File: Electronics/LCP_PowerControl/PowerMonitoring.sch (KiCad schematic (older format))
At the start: 18 parts, among them Q1 2N7002, Q2 2N7002, U1 MAX17205

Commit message: Adding libraries and recent changes
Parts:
- added J?: Conn_02x04_Odd_Even, Connector_PinSocket_2.54mm:PinSocket_2x04_P2.54mm_Vertical, symbol Connector_Generic:Conn_02x04_Odd_Even
- added TP? (x2): TestPoint, TestPoint:TestPoint_Keystone_5000-5004_Miniature, symbol Connector:TestPoint
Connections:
- wire segments 64 -> 82
- no-connect marks 0 -> 1
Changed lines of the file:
@@
 $Descr A4 11693 8268
 encoding utf-8
-Sheet 3 8
+Sheet 3 11
 Title ""
 Date ""
@@
 Connection ~ 5450 5300
 Wire Wire Line
-	1650 5300 5450 5300
+	1650 5300 3450 5300
 Text HLabel 1600 2300 0    50   Input ~ 0
 BATT_V+
@@
 BM_SDA
 Wire Wire Line
-	10350 3250 8900 3250
+	10350 3250 9600 3250
 Text HLabel 10350 3500 2    50   Input ~ 0
 BM_SCL
@@
 BM_IRQ
 Wire Wire Line
-	10350 3500 8900 3500
-Wire Wire Line
-	8900 3750 10350 3750
+	10350 3500 9500 3500
 Wire Wire Line
 	4000 3600 5400 3600
@@
 	8150 2300 8150 2050
 Wire Wire Line
-	4900 2300 8150 2300
+	4900 2300 6600 2300
+$Comp
+L power:GND #PWR?
+U 1 1 5EEDB371
+P 9400 5100
+AR Path="/5EE2AA1B/5EEDB371" Ref="#PWR?"  Part="1"
+AR Path="/5EE2A7AF/5EEDB371" Ref="#PWR?"  Part="1"
+F 0 "#PWR?" H 9400 4850 50  0001 C CNN
+F 1 "GND" H 9405 4927 50  0000 C CNN
+F 2 "" H 9400 5100 50  0001 C CNN
+F 3 "" H 9400 5100 50  0001 C CNN
+	1    9400 5100
+	1    0    0    -1
+$EndComp
+Wire Wire Line
+	9400 5100 9400 4950
+Wire Wire Line
+	9500 4900 9500 4950
+Wire Wire Line
+	9500 4950 9400 4950
+Connection ~ 9400 4950
+Wire Wire Line
+	9400 4950 9400 4900
+Wire Wire Line
+	9600 4900 9600 4950
+Connection ~ 9500 4950
+$Comp
+L Connector_Generic:Conn_02x04_Odd_Even J?
+U 1 1 5EEDB37F
+P 9500 4600
+AR Path="/5EE2AA1B/5EEDB37F" Ref="J?"  Part="1"
+AR Path="/5EE2A7AF/5EEDB37F" Ref="J?"  Part="1"
+F 0 "J?" V 9459 4312 50  0000 R CNN
+F 1 "Conn_02x04_Odd_Even" V 9550 4312 50  0000 R CNN
+F 2 "Connector_PinSocket_2.54mm:PinSocket_2x04_P2.54mm_Vertical" H 9500 4600 50  0001 C CNN
+F 3 "~" H 9500 4600 50  0001 C CNN
+F 4 "SALEAE_TEST" V 9641 4312 50  0000 R CNN "Field4"
+	1    9500 4600
+	0    -1   1    0
+$EndComp
+Wire Wire Line
+	9700 4900 9700 4950
+Wire Wire Line
+	9500 4950 9600 4950
+Wire Wire Line
+	9600 4950 9700 4950
+Connection ~ 9600 4950
+Wire Wire Line
+	9400 4400 9400 3750
+Wire Wire Line
+	8900 3750 9400 3750
+Connection ~ 9400 3750
+Wire Wire Line
+	9400 3750 10350 3750
+Wire Wire Line
+	9500 4400 9500 3500
+Connection ~ 9500 3500
+Wire Wire Line
+	9500 3500 8900 3500
+Wire Wire Line
+	9600 4400 9600 3250
+Connection ~ 9600 3250
+Wire Wire Line
+	9600 3250 8900 3250
+NoConn ~ 9700 4400
+$Comp
+L Connector:TestPoint TP?
+U 1 1 5EE905FF
+P 6600 2200
+F 0 "TP?" H 6658 2318 50  0000 L CNN
+F 1 "TestPoint" H 6658 2227 50  0000 L CNN
+F 2 "TestPoint:TestPoint_Keystone_5000-5004_Miniature" H 6800 2200 50  0001 C CNN
+F 3 "~" H 6800 2200 50  0001 C CNN
+F 4 "5000" H 6600 2200 50  0001 C CNN "MPN"
+	1    6600 2200
+	1    0    0    -1
+$EndComp
+Wire Wire Line
+	6600 2200 6600 2300
+Connection ~ 6600 2300
+Wire Wire Line
+	6600 2300 8150 2300
+$Comp
+L Connector:TestPoint TP?
+U 1 1 5EE92BE6
+P 3450 5250
+F 0 "TP?" H 3508 5368 50  0000 L CNN
+F 1 "TestPoint" H 3508 5277 50  0000 L CNN
+F 2 "TestPoint:TestPoint_Keystone_5000-5004_Miniature" H 3650 5250 50  0001 C CNN
+F 3 "~" H 3650 5250 50  0001 C CNN
+F 4 "5001" H 3450 5250 50  0001 C CNN "MPN"
+	1    3450 5250
+	1    0    0    -1
+$EndComp
+Wire Wire Line
+	3450 5250 3450 5300
+Connection ~ 3450 5300
+Wire Wire Line
+	3450 5300 5450 5300
 $EndSCHEMATC

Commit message: Aiming for rev 0.1 complete
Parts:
- R6, R7, R8: footprint (none) -> Resistor_SMD:R_0805_2012Metric
- gave numbers to parts that had none: 3
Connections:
- wire segments 82 -> 87
- no-connect marks 1 -> 4
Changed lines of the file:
@@
 Sheet 3 11
 Title ""
-Date ""
-Rev ""
+Date "2020-06-17"
+Rev "R0.1"
 Comp ""
-Comment1 ""
+Comment1 "Design by: Matt Casari"
 Comment2 ""
 Comment3 ""
@@
 F 0 "R6" V 8650 3250 50  0000 C CNN
 F 1 "1k" V 8750 3250 50  0000 C CNN
-F 2 "" V 8680 3250 50  0001 C CNN
+F 2 "Resistor_SMD:R_0805_2012Metric" V 8680 3250 50  0001 C CNN
 F 3 "~" H 8750 3250 50  0001 C CNN
 	1    8750 3250
@@
 F 0 "R7" V 8650 3500 50  0000 C CNN
 F 1 "150" V 8750 3500 50  0000 C CNN
-F 2 "" V 8680 3500 50  0001 C CNN
+F 2 "Resistor_SMD:R_0805_2012Metric" V 8680 3500 50  0001 C CNN
 F 3 "~" H 8750 3500 50  0001 C CNN
 	1    8750 3500
@@
 F 0 "R8" V 8650 3750 50  0000 C CNN
 F 1 "150" V 8750 3750 50  0000 C CNN
-F 2 "" V 8680 3750 50  0001 C CNN
+F 2 "Resistor_SMD:R_0805_2012Metric" V 8680 3750 50  0001 C CNN
 F 3 "~" H 8750 3750 50  0001 C CNN
 	1    8750 3750
@@
 	5050 3350 4900 3350
 Wire Wire Line
-	5400 3200 5200 3200
-Wire Wire Line
 	5200 3200 5200 3000
 Wire Wire Line
@@
 L power:+BATT #PWR07
 U 1 1 5EE801D6
-P 8150 2050
-F 0 "#PWR07" H 8150 1900 50  0001 C CNN
-F 1 "+BATT" H 8165 2223 50  0000 C CNN
-F 2 "" H 8150 2050 50  0001 C CNN
-F 3 "" H 8150 2050 50  0001 C CNN
-	1    8150 2050
-	1    0    0    -1
-$EndComp
-Wire Wire Line
-	8150 2300 8150 2050
+P 8150 2150
+F 0 "#PWR07" H 8150 2000 50  0001 C CNN
+F 1 "+BATT" H 8165 2323 50  0000 C CNN
+F 2 "" H 8150 2150 50  0001 C CNN
+F 3 "" H 8150 2150 50  0001 C CNN
+	1    8150 2150
+	1    0    0    -1
+$EndComp
+Wire Wire Line
+	8150 2300 8150 2150
 Wire Wire Line
 	4900 2300 6600 2300
@@
 P 9400 5100
 AR Path="/5EE2AA1B/5EEDB371" Ref="#PWR?"  Part="1"
-AR Path="/5EE2A7AF/5EEDB371" Ref="#PWR?"  Part="1"
-F 0 "#PWR?" H 9400 4850 50  0001 C CNN
+AR Path="/5EE2A7AF/5EEDB371" Ref="#PWR032"  Part="1"
+F 0 "#PWR032" H 9400 4850 50  0001 C CNN
 F 1 "GND" H 9405 4927 50  0000 C CNN
 F 2 "" H 9400 5100 50  0001 C CNN
@@
 P 9500 4600
 AR Path="/5EE2AA1B/5EEDB37F" Ref="J?"  Part="1"
-AR Path="/5EE2A7AF/5EEDB37F" Ref="J?"  Part="1"
-F 0 "J?" V 9459 4312 50  0000 R CNN
+AR Path="/5EE2A7AF/5EEDB37F" Ref="J13"  Part="1"
+F 0 "J13" V 9459 4312 50  0000 R CNN
 F 1 "Conn_02x04_Odd_Even" V 9550 4312 50  0000 R CNN
 F 2 "Connector_PinSocket_2.54mm:PinSocket_2x04_P2.54mm_Vertical" H 9500 4600 50  0001 C CNN
@@
 NoConn ~ 9700 4400
 $Comp
-L Connector:TestPoint TP?
+L Connector:TestPoint TP2
 U 1 1 5EE905FF
 P 6600 2200
-F 0 "TP?" H 6658 2318 50  0000 L CNN
+F 0 "TP2" H 6658 2318 50  0000 L CNN
 F 1 "TestPoint" H 6658 2227 50  0000 L CNN
 F 2 "TestPoint:TestPoint_Keystone_5000-5004_Miniature" H 6800 2200 50  0001 C CNN
@@
 Connection ~ 6600 2300
 Wire Wire Line
-	6600 2300 8150 2300
-$Comp
-L Connector:TestPoint TP?
+	6600 2300 7450 2300
+$Comp
+L Connector:TestPoint TP1
 U 1 1 5EE92BE6
 P 3450 5250
-F 0 "TP?" H 3508 5368 50  0000 L CNN
+F 0 "TP1" H 3508 5368 50  0000 L CNN
 F 1 "TestPoint" H 3508 5277 50  0000 L CNN
 F 2 "TestPoint:TestPoint_Keystone_5000-5004_Miniature" H 3650 5250 50  0001 C CNN
@@
 Wire Wire Line
 	3450 5300 5450 5300
+$Comp
+L power:PWR_FLAG #FLG0101
+U 1 1 5EEBFECA
+P 7450 2200
+F 0 "#FLG0101" H 7450 2275 50  0001 C CNN
+F 1 "PWR_FLAG" H 7450 2373 50  0000 C CNN
+F 2 "" H 7450 2200 50  0001 C CNN
+F 3 "~" H 7450 2200 50  0001 C CNN
+	1    7450 2200
+	1    0    0    -1
+$EndComp
+Wire Wire Line
+	7450 2200 7450 2300
+Connection ~ 7450 2300
+Wire Wire Line
+	7450 2300 8150 2300
+$Comp
+L power:PWR_FLAG #FLG0102
+U 1 1 5EEC41BF
+P 5550 2800
+F 0 "#FLG0102" H 5550 2875 50  0001 C CNN
+F 1 "PWR_FLAG" H 5550 2973 50  0000 C CNN
+F 2 "" H 5550 2800 50  0001 C CNN
+F 3 "~" H 5550 2800 50  0001 C CNN
+	1    5550 2800
+	1    0    0    -1
+$EndComp
+Wire Wire Line
+	5550 2800 5550 2900
+Wire Wire Line
+	5200 3200 5400 3200
+Wire Wire Line
+	5200 3000 5200 2900
+Wire Wire Line
+	5200 2900 5550 2900
+Connection ~ 5200 3000
+NoConn ~ 5400 4050
+NoConn ~ 5400 4200
+NoConn ~ 5400 4400
 $EndSCHEMATC

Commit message: KiCad Layout
Component and Traces finished. Need a look over. Will work on Silkscreen
after.

JTAG Connector. Should pin 1 be pulled up w/ 470Ohm resistor similar to
other designs? Also TDI and TMI signals are connected, is this correct?
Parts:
- U1: symbol PMEL_BatteryManagement:MAX17205 -> LCP_PowerControl-rescue:MAX17205-PMEL_BatteryManagement
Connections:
- wire segments 87 -> 86
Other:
- moved on the sheet: R5
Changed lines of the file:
@@
 $EndDescr
 $Comp
-L PMEL_BatteryManagement:MAX17205 U1
+L LCP_PowerControl-rescue:MAX17205-PMEL_BatteryManagement U1
 U 1 1 5EE2E9B5
 P 5950 3700
+AR Path="/5EE2E9B5" Ref="U1"  Part="1"
+AR Path="/5EE2A7AF/5EE2E9B5" Ref="U1"  Part="1"
 F 0 "U1" H 5925 4515 50  0000 C CNN
 F 1 "MAX17205" H 5925 4424 50  0000 C CNN
@@
 L Device:R R5
 U 1 1 5EE309A9
-P 5700 5300
-F 0 "R5" V 5600 5300 50  0000 C CNN
-F 1 "0.25" V 5800 5300 50  0000 C CNN
-F 2 "Resistor_THT:R_Axial_Power_L48.0mm_W12.5mm_P55.88mm" V 5630 5300 50  0001 C CNN
-F 3 "~" H 5700 5300 50  0001 C CNN
-F 4 "RS010R2500FE73" V 5700 5300 50  0001 C CNN "MPN"
-F 5 "10W" V 5700 5300 50  0000 C CNN "Power"
-	1    5700 5300
-	0    1    1    0
-$EndComp
-Wire Wire Line
-	5850 5300 6200 5300
+P 5950 5300
+F 0 "R5" V 5850 5300 50  0000 C CNN
+F 1 "0.25" V 6050 5300 50  0000 C CNN
+F 2 "Resistor_THT:R_Axial_Power_L48.0mm_W12.5mm_P55.88mm" V 5880 5300 50  0001 C CNN
+F 3 "~" H 5950 5300 50  0001 C CNN
+F 4 "RS010R2500FE73" V 5950 5300 50  0001 C CNN "MPN"
+F 5 "10W" V 5950 5300 50  0000 C CNN "Power"
+	1    5950 5300
+	0    1    1    0
+$EndComp
+Wire Wire Line
+	6100 5300 6200 5300
 Connection ~ 6200 5300
 Wire Wire Line
-	5700 5000 5450 5000
-Wire Wire Line
-	5450 5000 5450 5300
-Wire Wire Line
-	5450 5300 5550 5300
-Wire Wire Line
-	5950 5000 5700 5000
-Connection ~ 5700 5000
+	5700 5300 5800 5300
 $Comp
 L Transistor_FET:2N7002 Q1
@@
 Text HLabel 1650 5300 0    50   Output ~ 0
 BATT_V-
-Connection ~ 5450 5300
+Connection ~ 5700 5300
 Wire Wire Line
 	1650 5300 3450 5300
@@
 Connection ~ 3700 3800
 Wire Wire Line
-	6200 4850 6200 5300
-Wire Wire Line
-	5950 4850 5950 5000
-Wire Wire Line
-	5700 4850 5700 5000
+	6200 4850 6200 5000
 $Comp
 L power:GND #PWR01
@@
 Connection ~ 3450 5300
 Wire Wire Line
-	3450 5300 5450 5300
+	3450 5300 5700 5300
 $Comp
 L power:PWR_FLAG #FLG0101
@@
 NoConn ~ 5400 4200
 NoConn ~ 5400 4400
+Wire Wire Line
+	5950 4850 5950 5000
+Wire Wire Line
+	5950 5000 6200 5000
+Connection ~ 6200 5000
+Wire Wire Line
+	6200 5000 6200 5300
+Wire Wire Line
+	5700 4850 5700 5300
 $EndSCHEMATC

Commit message: Position request within 0.005 inches working
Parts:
- U1: symbol LCP_PowerControl-rescue:MAX17205-PMEL_BatteryManagement -> LCP_PowerControl-rescue:MAX17205-PMEL_BatteryManagement-LCP_PowerControl-rescue
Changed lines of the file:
@@
 $EndDescr
 $Comp
-L LCP_PowerControl-rescue:MAX17205-PMEL_BatteryManagement U1
+L LCP_PowerControl-rescue:MAX17205-PMEL_BatteryManagement-LCP_PowerControl-rescue U1
 U 1 1 5EE2E9B5
 P 5950 3700

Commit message: LCP_PowerControl Rev1
Board layout in Kicad.
Gerbers.
BOM
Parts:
- C1: MPN (none) -> C1206X7R101-105KNE
- C2, C3: MPN (none) -> 885012207102
- R3: MPN (none) -> CRCW0805200KJNEA
- R6: MPN (none) -> RNCP0805FTD1K00
- R7, R8: MPN (none) -> RNCP0805FTD150R
- renumbered Q1 to e
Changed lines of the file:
@@
 	5700 5300 5800 5300
 $Comp
-L Transistor_FET:2N7002 Q1
+L Transistor_FET:2N7002 e
 U 1 1 5EE31D3D
 P 3800 3600
-F 0 "Q1" H 4005 3646 50  0000 L CNN
+F 0 "e" H 4005 3646 50  0000 L CNN
 F 1 "2N7002" H 4005 3555 50  0000 L CNN
 F 2 "Package_TO_SOT_SMD:SOT-23" H 4000 3525 50  0001 L CIN
@@
 F 2 "Resistor_SMD:R_0805_2012Metric" V 8680 3250 50  0001 C CNN
 F 3 "~" H 8750 3250 50  0001 C CNN
+F 4 "RNCP0805FTD1K00" V 8750 3250 50  0001 C CNN "MPN"
 	1    8750 3250
 	0    1    1    0
@@
 F 2 "Resistor_SMD:R_0805_2012Metric" V 8680 3500 50  0001 C CNN
 F 3 "~" H 8750 3500 50  0001 C CNN
+F 4 "RNCP0805FTD150R" V 8750 3500 50  0001 C CNN "MPN"
 	1    8750 3500
 	0    1    1    0
@@
 F 2 "Resistor_SMD:R_0805_2012Metric" V 8680 3750 50  0001 C CNN
 F 3 "~" H 8750 3750 50  0001 C CNN
+F 4 "RNCP0805FTD150R" V 8750 3750 50  0001 C CNN "MPN"
 	1    8750 3750
 	0    1    1    0
@@
 F 2 "Resistor_SMD:R_0805_2012Metric" V 3630 4050 50  0001 C CNN
 F 3 "~" H 3700 4050 50  0001 C CNN
+F 4 "CRCW0805200KJNEA" H 3700 4050 50  0001 C CNN "MPN"
 	1    3700 4050
 	1    0    0    -1
@@
 	1    0    0    -1
 $EndComp
-$Comp
-L Device:R R4
-U 1 1 5EE5DDEB
-P 4350 2550
-F 0 "R4" H 4420 2596 50  0000 L CNN
-F 1 "500k" H 4420 2505 50  0000 L CNN
-F 2 "Resistor_SMD:R_0805_2012Metric" V 4280 2550 50  0001 C CNN
-F 3 "~" H 4350 2550 50  0001 C CNN
-F 4 "CRCW08058M87FKEA" H 4350 2550 50  0001 C CNN "MPN"
-	1    4350 2550
-	1    0    0    -1
-$EndComp
 Wire Wire Line
 	4600 2750 4350 2750
@@
 F 2 "Capacitor_SMD:C_0805_2012Metric" H 6738 4450 50  0001 C CNN
 F 3 "~" H 6700 4600 50  0001 C CNN
+F 4 "885012207102" H 6700 4600 50  0001 C CNN "MPN"
 	1    6700 4600
 	1    0    0    -1
@@
 F 2 "Capacitor_SMD:C_0805_2012Metric" H 7188 4450 50  0001 C CNN
 F 3 "~" H 7150 4600 50  0001 C CNN
+F 4 "885012207102" H 7150 4600 50  0001 C CNN "MPN"
 	1    7150 4600
 	1    0    0    -1
@@
 F 2 "Capacitor_SMD:C_0805_2012Metric" H 4938 3000 50  0001 C CNN
 F 3 "~" H 4900 3150 50  0001 C CNN
+F 4 "C1206X7R101-105KNE" H 4900 3150 50  0001 C CNN "MPN"
 	1    4900 3150
 	1    0    0    -1
@@
 Wire Wire Line
 	5700 4850 5700 5300
+$Comp
+L Device:R R4
+U 1 1 5EE5DDEB
+P 4350 2550
+F 0 "R4" H 4420 2596 50  0000 L CNN
+F 1 "500k" H 4420 2505 50  0000 L CNN
+F 2 "Resistor_SMD:R_0805_2012Metric" V 4280 2550 50  0001 C CNN
+F 3 "~" H 4350 2550 50  0001 C CNN
+F 4 "CRCW08058M87FKEA" H 4350 2550 50  0001 C CNN "MPN"
+	1    4350 2550
+	1    0    0    -1
+$EndComp
 $EndSCHEMATC

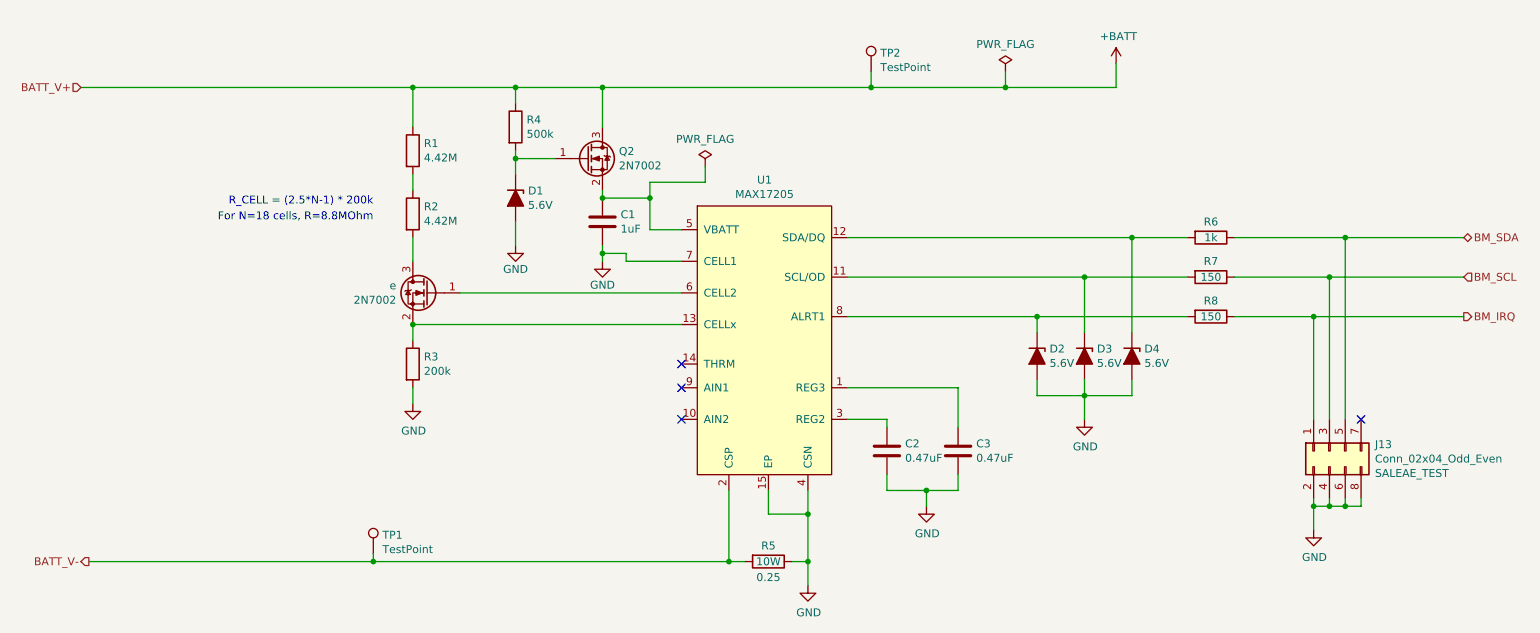
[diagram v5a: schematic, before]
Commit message: Rev1
Removed test points. Cleaned up unnecessary traces. Fixed electrical issues #1-#7
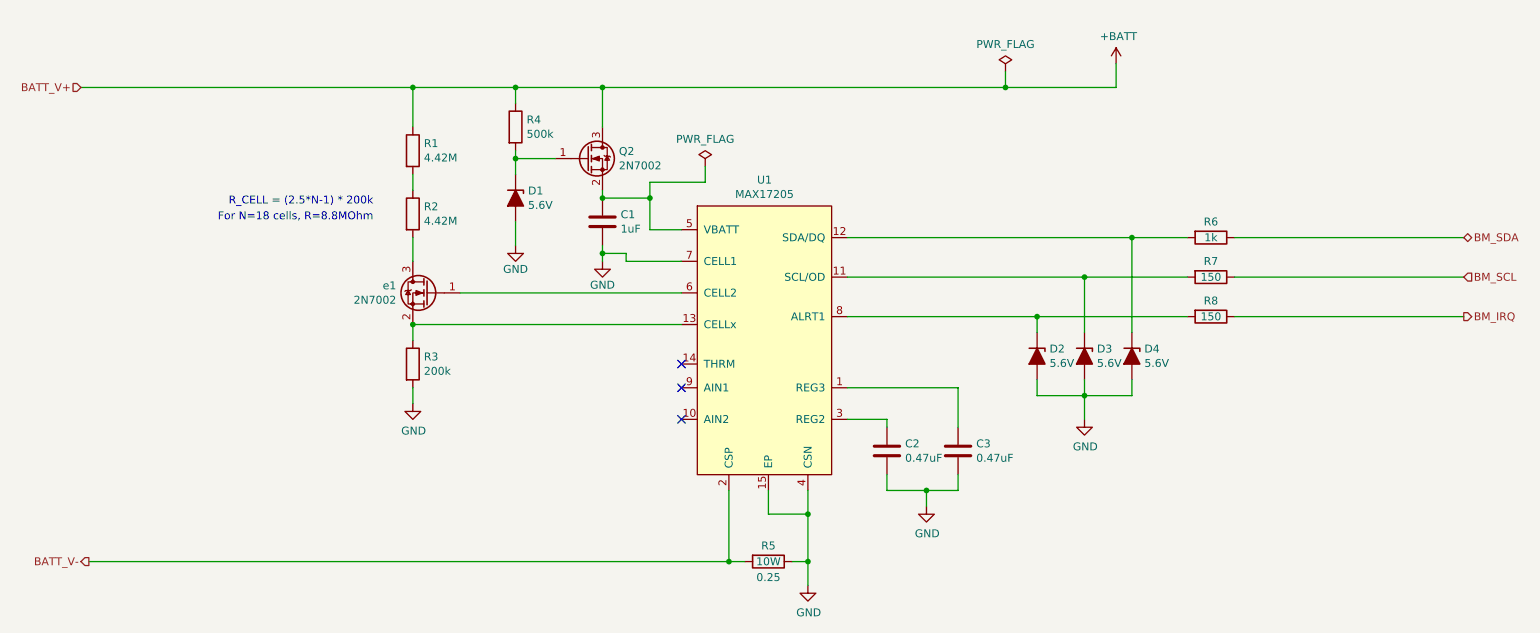
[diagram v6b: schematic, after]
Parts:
- removed J13: Conn_02x04_Odd_Even, Connector_PinSocket_2.54mm:PinSocket_2x04_P2.54mm_Vertical, symbol Connector_Generic:Conn_02x04_Odd_Even
- removed TP1, TP2: TestPoint, TestPoint:TestPoint_Keystone_5000-5004_Miniature, symbol Connector:TestPoint
- renumbered e to e1
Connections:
- no-connect marks 4 -> 3
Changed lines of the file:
@@
 	5700 5300 5800 5300
 $Comp
-L Transistor_FET:2N7002 e
+L Transistor_FET:2N7002 e1
 U 1 1 5EE31D3D
 P 3800 3600
-F 0 "e" H 4005 3646 50  0000 L CNN
+F 0 "e1" H 4005 3646 50  0000 L CNN
 F 1 "2N7002" H 4005 3555 50  0000 L CNN
 F 2 "Package_TO_SOT_SMD:SOT-23" H 4000 3525 50  0001 L CIN
@@
 BATT_V-
 Connection ~ 5700 5300
-Wire Wire Line
-	1650 5300 3450 5300
 Text HLabel 1600 2300 0    50   Input ~ 0
 BATT_V+
@@
 Text HLabel 10350 3250 2    50   BiDi ~ 0
 BM_SDA
-Wire Wire Line
-	10350 3250 9600 3250
 Text HLabel 10350 3500 2    50   Input ~ 0
 BM_SCL
 Text HLabel 10350 3750 2    50   Output ~ 0
 BM_IRQ
-Wire Wire Line
-	10350 3500 9500 3500
 Wire Wire Line
 	4000 3600 5400 3600
@@
 Wire Wire Line
 	8150 2300 8150 2150
-Wire Wire Line
-	4900 2300 6600 2300
-$Comp
-L power:GND #PWR?
-U 1 1 5EEDB371
-P 9400 5100
-AR Path="/5EE2AA1B/5EEDB371" Ref="#PWR?"  Part="1"
-AR Path="/5EE2A7AF/5EEDB371" Ref="#PWR032"  Part="1"
-F 0 "#PWR032" H 9400 4850 50  0001 C CNN
-F 1 "GND" H 9405 4927 50  0000 C CNN
-F 2 "" H 9400 5100 50  0001 C CNN
-F 3 "" H 9400 5100 50  0001 C CNN
-	1    9400 5100
-	1    0    0    -1
-$EndComp
-Wire Wire Line
-	9400 5100 9400 4950
-Wire Wire Line
-	9500 4900 9500 4950
-Wire Wire Line
-	9500 4950 9400 4950
-Connection ~ 9400 4950
-Wire Wire Line
-	9400 4950 9400 4900
-Wire Wire Line
-	9600 4900 9600 4950
-Connection ~ 9500 4950
-$Comp
-L Connector_Generic:Conn_02x04_Odd_Even J?
-U 1 1 5EEDB37F
-P 9500 4600
-AR Path="/5EE2AA1B/5EEDB37F" Ref="J?"  Part="1"
-AR Path="/5EE2A7AF/5EEDB37F" Ref="J13"  Part="1"
-F 0 "J13" V 9459 4312 50  0000 R CNN
-F 1 "Conn_02x04_Odd_Even" V 9550 4312 50  0000 R CNN
-F 2 "Connector_PinSocket_2.54mm:PinSocket_2x04_P2.54mm_Vertical" H 9500 4600 50  0001 C CNN
-F 3 "~" H 9500 4600 50  0001 C CNN
-F 4 "SALEAE_TEST" V 9641 4312 50  0000 R CNN "Field4"
-	1    9500 4600
-	0    -1   1    0
-$EndComp
-Wire Wire Line
-	9700 4900 9700 4950
-Wire Wire Line
-	9500 4950 9600 4950
-Wire Wire Line
-	9600 4950 9700 4950
-Connection ~ 9600 4950
-Wire Wire Line
-	9400 4400 9400 3750
-Wire Wire Line
-	8900 3750 9400 3750
-Connection ~ 9400 3750
-Wire Wire Line
-	9400 3750 10350 3750
-Wire Wire Line
-	9500 4400 9500 3500
-Connection ~ 9500 3500
-Wire Wire Line
-	9500 3500 8900 3500
-Wire Wire Line
-	9600 4400 9600 3250
-Connection ~ 9600 3250
-Wire Wire Line
-	9600 3250 8900 3250
-NoConn ~ 9700 4400
-$Comp
-L Connector:TestPoint TP2
-U 1 1 5EE905FF
-P 6600 2200
-F 0 "TP2" H 6658 2318 50  0000 L CNN
-F 1 "TestPoint" H 6658 2227 50  0000 L CNN
-F 2 "TestPoint:TestPoint_Keystone_5000-5004_Miniature" H 6800 2200 50  0001 C CNN
-F 3 "~" H 6800 2200 50  0001 C CNN
-F 4 "5000" H 6600 2200 50  0001 C CNN "MPN"
-	1    6600 2200
-	1    0    0    -1
-$EndComp
-Wire Wire Line
-	6600 2200 6600 2300
-Connection ~ 6600 2300
-Wire Wire Line
-	6600 2300 7450 2300
-$Comp
-L Connector:TestPoint TP1
-U 1 1 5EE92BE6
-P 3450 5250
-F 0 "TP1" H 3508 5368 50  0000 L CNN
-F 1 "TestPoint" H 3508 5277 50  0000 L CNN
-F 2 "TestPoint:TestPoint_Keystone_5000-5004_Miniature" H 3650 5250 50  0001 C CNN
-F 3 "~" H 3650 5250 50  0001 C CNN
-F 4 "5001" H 3450 5250 50  0001 C CNN "MPN"
-	1    3450 5250
-	1    0    0    -1
-$EndComp
-Wire Wire Line
-	3450 5250 3450 5300
-Connection ~ 3450 5300
-Wire Wire Line
-	3450 5300 5700 5300
 $Comp
 L power:PWR_FLAG #FLG0101
@@
 	1    0    0    -1
 $EndComp
+Wire Wire Line
+	8900 3750 10350 3750
+Wire Wire Line
+	8900 3500 10350 3500
+Wire Wire Line
+	8900 3250 10350 3250
+Wire Wire Line
+	1650 5300 5700 5300
+Wire Wire Line
+	4900 2300 7450 2300
 $EndSCHEMATC
